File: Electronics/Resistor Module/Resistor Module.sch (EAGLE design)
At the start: 59 parts, among them IC1 74HC595D, IC2 74HC595D, U1 25AA010A

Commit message: Finished layout of resistor module
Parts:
- removed JP5, JP6, JP7, JP8: (no value), Resistor Module Library:M03X24-103240-0-03
- JP1, JP2: value (none) -> M10PASSTHROUGH; device Resistor Module Library:M03X2_535542-3 -> Resistor Module Library:M10PASSTHROUGH
- JP3: device Resistor Module Library:M03X2_535542-3 -> Resistor Module Library:M03X2969973-3
- JP4: device Resistor Module Library:M03X2_535542-3 -> Resistor Module Library:M03X2SMT-M0.1
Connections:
- net N$1 renamed SERIAL_PASS
- removed net N$20 (its old number): IC1A.QG, R19.1
- removed net N$27: IC2A.QE, R25.1
- removed net N$28: IC2A.QF, R26.1
- new net 5V_2: IC2P.VCC, JP2.6
- new net GND_2: IC2P.GND, JP2.5, S10.C-, S11.C-, S12.C-, S13.C-, S7.C-, S8.C-, S9.C-
- new net N$1: IC1A.QH, R26.1
- new net N$13: IC1A.QE, R16.1
- new net N$14: IC1A.QD, R17.1
- new net SERIAL_CLK_2: IC2A.SCK, JP2.9
- new net SERIAL_LATCH_2: IC2A.RCK, JP2.8
- new net SERIAL_MR_L_2: IC2A.SCL, JP2.10
- new net SERIAL_OE_L_2: IC2A.G, JP2.7
- net 5V: now also JP1.6; no longer IC2P.VCC, JP4.1, JP8.5
- net EEPROM_CS_L: now also IC1A.QA; no longer IC2A.QG
- net EEPROM_MISO: now also JP1.4; no longer JP4.4, JP8.4
- net EEPROM_MOSI: now also JP1.2; no longer JP4.2, JP8.6
- net EEPROM_SCK: now also JP1.3; no longer JP4.6, JP8.2
- net GND: now also JP1.5; no longer IC2P.GND, JP4.5, JP8.1, S10.C-, S11.C-, S12.C-, S13.C-, S7.C-, S8.C-, S9.C-
- net N$12: now also IC1A.QF, R15.1; no longer IC1A.QB, R14.1
- net N$16: now also R18.1; no longer R15.1
- net N$17: now also IC1A.QB, R19.1; no longer IC1A.QD, R16.1
- net N$18: now also IC2A.QB, R13.1; no longer IC1A.QE, R17.1
- net N$19: now also IC2A.QC, R25.1; no longer IC1A.QF, R18.1
- net N$2: now also IC1A.QG, R14.1; no longer IC1A.QA, R13.1
- net N$21: now also IC2A.QE, R23.1; no longer IC1A.QH, R20.1
- net N$22: now also IC2A.QF, R22.1; no longer IC2A.QA, R21.1
- net N$23: now also IC2A.QG, R21.1; no longer IC2A.QB, R22.1
- net N$24: now also IC2A.QH, R20.1; no longer IC2A.QC, R23.1
- net RELAY_POST_SHORT: now also S0.C+; no longer S13.C+
- net RELAY_PRE_SHORT: now also S13.C+; no longer S0.C+
- net R_DOWNSTREAM_IN: now also JP3.1, R12.1, R120.1, S12.DC-, S13.DC-; no longer JP3.5, JP3.6, R1.2, S0.DC+, S1.DC+
- net R_DOWNSTREAM_OUT: now also JP4.1, R1.2, S0.DC+, S1.DC+; no longer JP7.1, JP7.2, R12.1, R120.1, S12.DC-, S13.DC-
- net R_UPSTREAM: now also JP3.6, JP4.2; no longer JP3.1, JP3.2, JP7.5, JP7.6
- net SERIAL_CLK: now also JP1.9; no longer IC2A.SCK, JP2.3, JP6.3
- net SERIAL_IN: now also JP3.2; no longer JP2.1
- net SERIAL_LATCH: now also JP1.8; no longer IC2A.RCK, JP2.5, JP6.1
- net SERIAL_MR_L: now also JP1.10; no longer IC2A.SCL, JP2.6, JP6.2
- net SERIAL_OE_L: now also JP1.7; no longer IC2A.G, JP2.4, JP6.4
- net SERIAL_OUT: now also JP4.6; no longer JP6.5
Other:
- note added: "BOTTOM"
- note added: "TOP"
- note removed: "Bottom"
- note removed: "Top"
- moved on the sheet: JP1, JP2, JP3, JP4, R13, R14, R15, R16, R17, R18, R19, R20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

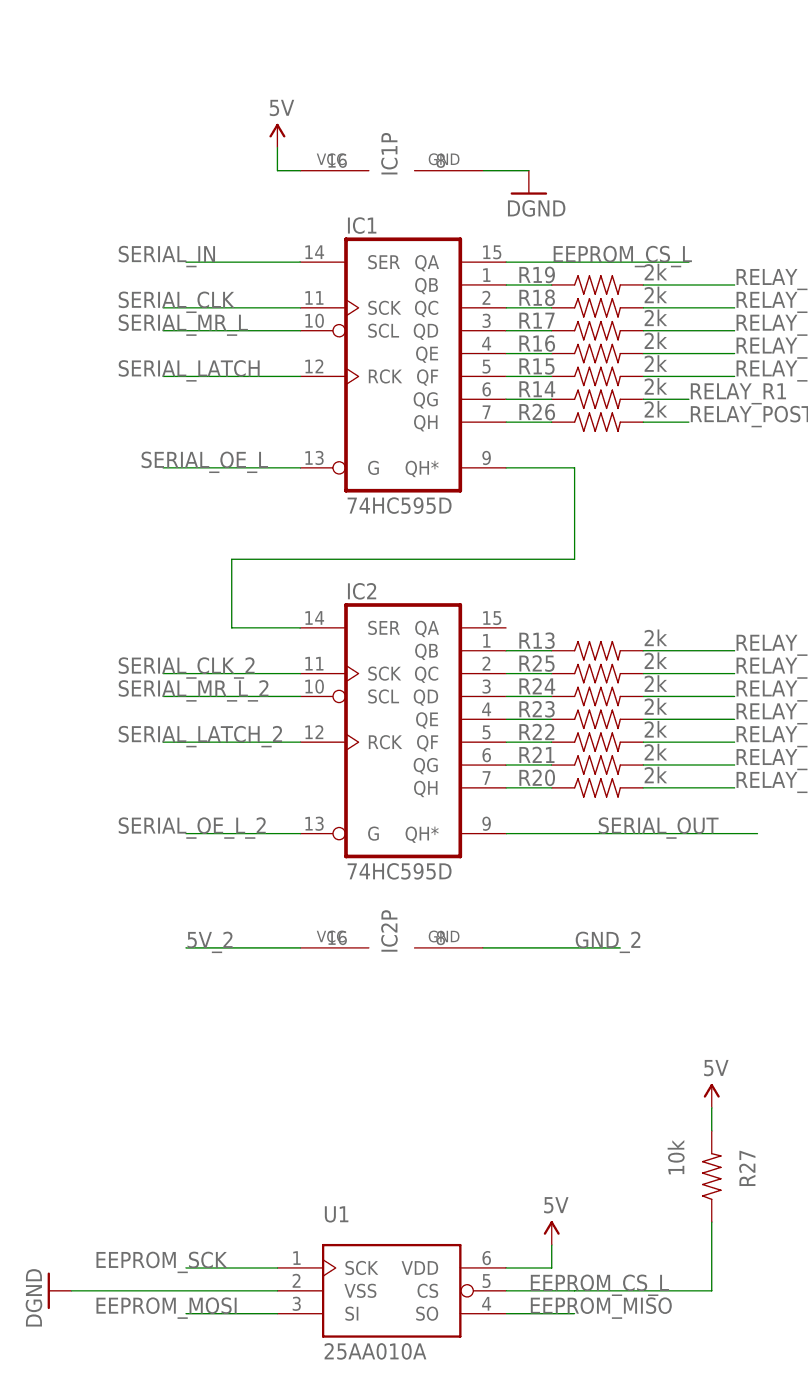
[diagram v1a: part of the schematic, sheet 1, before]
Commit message: Finished layout and updated sketch. Discovered I could fit entire range on a single node if I double back the thing, so gonna do that instead. Who needs modularity when the entire thing fits on one board?
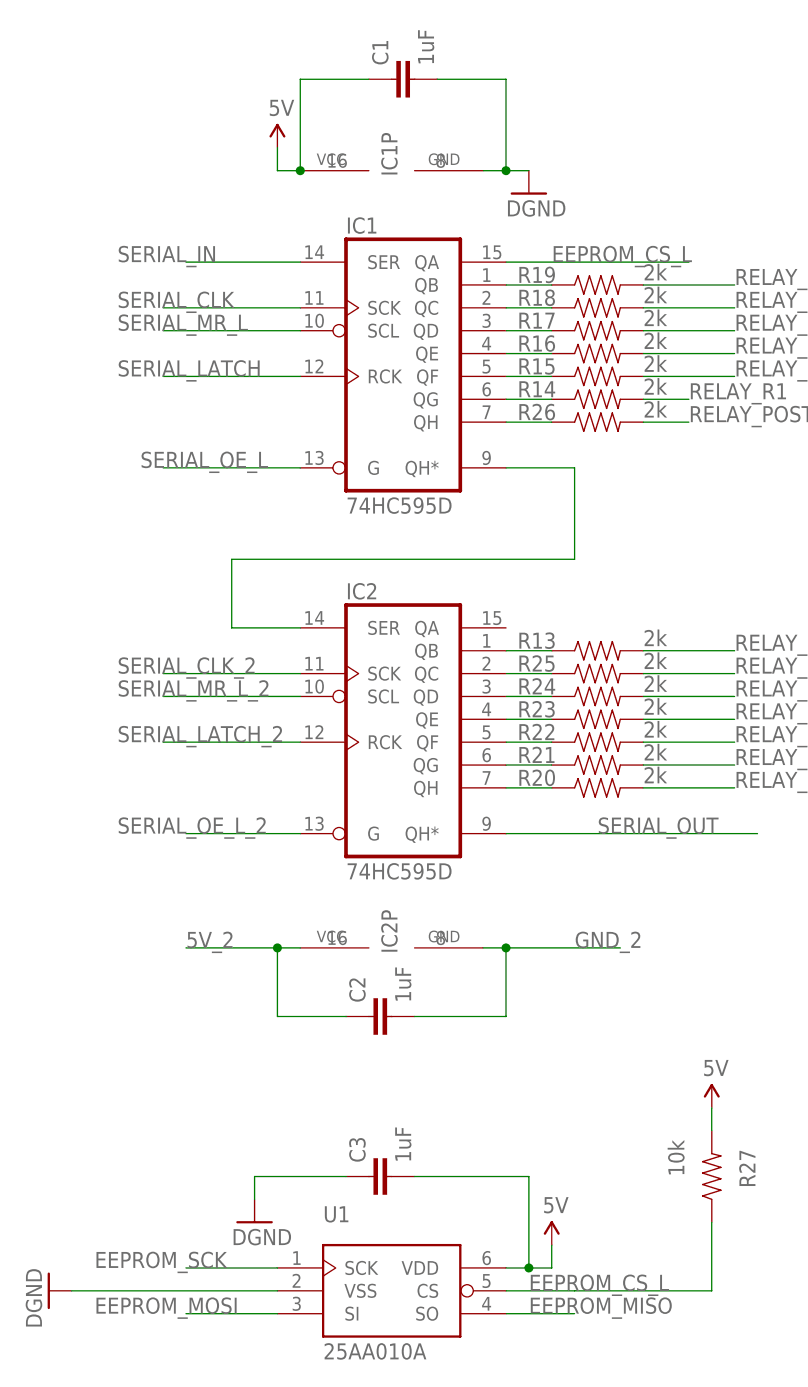
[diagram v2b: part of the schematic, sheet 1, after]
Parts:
- added C1, C2, C3: 1uF, Resistor Module Library:CAP0603-CAP
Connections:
- net 5V: now also C1.1, C3.2
- net 5V_2: now also C2.1
- net GND: now also C1.2, C3.1
- net GND_2: now also C2.2
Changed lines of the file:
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@@
 <part name="SUPPLY6" library="Resistor Module Library" deviceset="5V" device=""/>
 <part name="GND19" library="Resistor Module Library" deviceset="DGND" device=""/>
+<part name="C1" library="Resistor Module Library" deviceset="CAP" device="0603-CAP" value="1uF"/>
+<part name="C2" library="Resistor Module Library" deviceset="CAP" device="0603-CAP" value="1uF"/>
+<part name="C3" library="Resistor Module Library" deviceset="CAP" device="0603-CAP" value="1uF"/>
+<part name="GND2" library="Resistor Module Library" deviceset="DGND" device=""/>
 </parts>
 <sheets>
@@
 </instance>
 <instance part="SUPPLY4" gate="G$1" x="35.56" y="-83.82"/>
+<instance part="C1" gate="G$1" x="2.54" y="30.48" rot="R90"/>
+<instance part="C2" gate="G$1" x="0" y="-73.66" rot="R90"/>
+<instance part="C3" gate="G$1" x="0" y="-91.44" rot="R90"/>
+<instance part="GND2" gate="G$1" x="-15.24" y="-96.52"/>
 </instances>
 <busses>
@@
 <wire x1="-10.16" y1="20.32" x2="-12.7" y2="20.32" width="0.1524" layer="91"/>
 <wire x1="-12.7" y1="20.32" x2="-12.7" y2="22.86" width="0.1524" layer="91"/>
+<pinref part="C1" gate="G$1" pin="1"/>
+<wire x1="-2.54" y1="30.48" x2="-10.16" y2="30.48" width="0.1524" layer="91"/>
+<wire x1="-10.16" y1="30.48" x2="-10.16" y2="20.32" width="0.1524" layer="91"/>
+<junction x="-10.16" y="20.32"/>
 </segment>
 <segment>
 <pinref part="U1" gate="G$1" pin="VDD"/>
-<wire x1="12.7" y1="-101.6" x2="17.78" y2="-101.6" width="0.1524" layer="91"/>
+<wire x1="12.7" y1="-101.6" x2="15.24" y2="-101.6" width="0.1524" layer="91"/>
+<wire x1="15.24" y1="-101.6" x2="17.78" y2="-101.6" width="0.1524" layer="91"/>
 <wire x1="17.78" y1="-101.6" x2="17.78" y2="-99.06" width="0.1524" layer="91"/>
 <pinref part="SUPPLY3" gate="G$1" pin="5V"/>
+<pinref part="C3" gate="G$1" pin="2"/>
+<wire x1="2.54" y1="-91.44" x2="15.24" y2="-91.44" width="0.1524" layer="91"/>
+<wire x1="15.24" y1="-91.44" x2="15.24" y2="-101.6" width="0.1524" layer="91"/>
+<junction x="15.24" y="-101.6"/>
 </segment>
 <segment>
@@
 <pinref part="GND1" gate="G$1" pin="GND"/>
 <pinref part="IC1" gate="P" pin="GND"/>
-<wire x1="15.24" y1="20.32" x2="10.16" y2="20.32" width="0.1524" layer="91"/>
+<wire x1="15.24" y1="20.32" x2="12.7" y2="20.32" width="0.1524" layer="91"/>
+<pinref part="C1" gate="G$1" pin="2"/>
+<wire x1="12.7" y1="20.32" x2="10.16" y2="20.32" width="0.1524" layer="91"/>
+<wire x1="5.08" y1="30.48" x2="12.7" y2="30.48" width="0.1524" layer="91"/>
+<wire x1="12.7" y1="30.48" x2="12.7" y2="20.32" width="0.1524" layer="91"/>
+<junction x="12.7" y="20.32"/>
 </segment>
 <segment>
@@
 <wire x1="-12.7" y1="-104.14" x2="-35.56" y2="-104.14" width="0.1524" layer="91"/>
 <pinref part="GND17" gate="G$1" pin="GND"/>
+</segment>
+<segment>
+<pinref part="C3" gate="G$1" pin="1"/>
+<wire x1="-5.08" y1="-91.44" x2="-15.24" y2="-91.44" width="0.1524" layer="91"/>
+<wire x1="-15.24" y1="-91.44" x2="-15.24" y2="-93.98" width="0.1524" layer="91"/>
+<pinref part="GND2" gate="G$1" pin="GND"/>
 </segment>
 </net>
@@
 <segment>
 <pinref part="IC2" gate="P" pin="VCC"/>
-<wire x1="-10.16" y1="-66.04" x2="-22.86" y2="-66.04" width="0.1524" layer="91"/>
+<wire x1="-10.16" y1="-66.04" x2="-12.7" y2="-66.04" width="0.1524" layer="91"/>
 <label x="-22.86" y="-66.04" size="1.778" layer="95"/>
+<pinref part="C2" gate="G$1" pin="1"/>
+<wire x1="-12.7" y1="-66.04" x2="-22.86" y2="-66.04" width="0.1524" layer="91"/>
+<wire x1="-5.08" y1="-73.66" x2="-12.7" y2="-73.66" width="0.1524" layer="91"/>
+<wire x1="-12.7" y1="-73.66" x2="-12.7" y2="-66.04" width="0.1524" layer="91"/>
+<junction x="-12.7" y="-66.04"/>
 </segment>
 </net>
@@
 <segment>
 <pinref part="IC2" gate="P" pin="GND"/>
-<wire x1="10.16" y1="-66.04" x2="25.4" y2="-66.04" width="0.1524" layer="91"/>
+<wire x1="10.16" y1="-66.04" x2="12.7" y2="-66.04" width="0.1524" layer="91"/>
 <label x="20.32" y="-66.04" size="1.778" layer="95"/>
-</segment>
-</net>
+<pinref part="C2" gate="G$1" pin="2"/>
+<wire x1="12.7" y1="-66.04" x2="25.4" y2="-66.04" width="0.1524" layer="91"/>
+<wire x1="2.54" y1="-73.66" x2="12.7" y2="-73.66" width="0.1524" layer="91"/>
+<wire x1="12.7" y1="-73.66" x2="12.7" y2="-66.04" width="0.1524" layer="91"/>
+<junction x="12.7" y="-66.04"/>
+</segment>
+</net>

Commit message: Reworking resistor module to fit everything on a single module
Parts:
- removed R120: 1k, Resistor Module Library:RESISTOR1206
- removed R80: 100, Resistor Module Library:RESISTOR1206
- removed S0: CPC1002N, Resistor Module Library:CPC1002N
- removed U1: 25AA010A, Resistor Module Library:25AA010A
- added $1_75_$: 25AA010A, Resistor Module Library:25AA010A
- added C4, C5: 1uF, Resistor Module Library:CAP0603-CAP
- added IC3, IC4: 74HC595D, Resistor Module Library:74HC595D
- added R28: 10k, Resistor Module Library:RESISTOR1206
- added R29: 100k, Resistor Module Library:RESISTOR1206
- added R30, R60: 1M, Resistor Module Library:RESISTOR1206
- added R31, R32, R33, R34, R35, R36, R37, R38, R39, R41, R42, R43, R44, R45, R46, R47, R48, R49, R50, R51, R52, R53, R54, R55, R56, R57, R58: 2k, Resistor Module Library:RESISTOR0603-RES
- added R59: 10k, Resistor Module Library:RESISTOR0603-RES
- added R61, R62: 2M, Resistor Module Library:RESISTOR1206
- added R63, R64: 10M, Resistor Module Library:RESISTOR1206
- added S14, S15, S16, S17, S18, S19, S20, S21, S22, S23, S24, S25, S26, S27, S28: CPC1002N, Resistor Module Library:CPC1002N
- JP2: value M10PASSTHROUGH -> (none); device Resistor Module Library:M10PASSTHROUGH -> Resistor Module Library:M03X2969973-3
- JP3: device Resistor Module Library:M03X2969973-3 -> Resistor Module Library:M03X2SMT-M0.1
- JP4: value (none) -> M10PASSTHROUGH; device Resistor Module Library:M03X2SMT-M0.1 -> Resistor Module Library:M10PASSTHROUGH
- R13: value 2k -> 1k; device Resistor Module Library:RESISTOR0603-RES -> Resistor Module Library:RESISTOR1206
- R14, R15: device Resistor Module Library:RESISTOR0603-RES -> Resistor Module Library:RESISTOR1206
- R16, R17: value 2k -> 10k; device Resistor Module Library:RESISTOR0603-RES -> Resistor Module Library:RESISTOR1206
- R18, R19: value 2k -> 20k; device Resistor Module Library:RESISTOR0603-RES -> Resistor Module Library:RESISTOR1206
- R20, R21: value 2k -> 100k; device Resistor Module Library:RESISTOR0603-RES -> Resistor Module Library:RESISTOR1206
- R22, R23: value 2k -> 200k; device Resistor Module Library:RESISTOR0603-RES -> Resistor Module Library:RESISTOR1206
- R24: value 2k -> 1M; device Resistor Module Library:RESISTOR0603-RES -> Resistor Module Library:RESISTOR1206
- R25: value 2k -> 10; device Resistor Module Library:RESISTOR0603-RES -> Resistor Module Library:RESISTOR1206
- R26: value 2k -> 100; device Resistor Module Library:RESISTOR0603-RES -> Resistor Module Library:RESISTOR1206
- R27: value 10k -> 1k; device Resistor Module Library:RESISTOR0603-RES -> Resistor Module Library:RESISTOR1206
- R40: value 10 -> 2k; device Resistor Module Library:RESISTOR1206 -> Resistor Module Library:RESISTOR0603-RES
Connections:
- new net N$26: IC3A.QH, R51.1
- new net N$27: IC3A.QG, R50.1
- new net N$28: IC3A.QF, R49.1
- new net N$29: IC3A.QE, R48.1
- new net N$30: IC3A.QD, R47.1
- new net N$31: IC3A.QC, R46.1
- new net N$32: IC3A.QB, R45.1
- new net N$33: IC4A.QB, R52.1
- new net N$34: IC4A.QC, R53.1
- new net N$35: IC4A.QD, R54.1
- new net N$36: IC4A.QE, R55.1
- new net N$37: IC4A.QF, R56.1
- new net N$38: IC4A.QG, R57.1
- new net N$39: IC4A.QH, R58.1
- new net N$40: R12.1, R13.2, R27.1, S12.DC-, S13.DC+
- new net N$41: R14.1, R15.2, S14.DC-, S15.DC+
- new net N$42: R15.1, R16.2, R28.2, S15.DC-, S16.DC+
- new net N$43: R16.1, R17.2, R28.1, S16.DC-, S17.DC+
- new net N$44: R17.1, R18.2, S17.DC-, S18.DC+
- new net N$45: R18.1, R19.2, S18.DC-, S19.DC+
- new net N$46: R19.1, R20.2, R29.2, S19.DC-, S20.DC+
- new net N$47: R20.1, R21.2, R29.1, S20.DC-, S21.DC+
- new net N$48: R21.1, R22.2, S21.DC-, S22.DC+
- new net N$49: R22.1, R23.2, S22.DC-, S23.DC+
- new net N$50: R23.1, R24.2, R30.2, S23.DC-, S24.DC+
- new net N$51: R13.1, R14.2, S13.DC-, S14.DC+
- new net N$52: R24.1, R30.1, R60.2, S24.DC-, S25.DC+
- new net N$54: R60.1, R61.2, S25.DC-, S26.DC+
- new net N$55: R61.1, R62.2, S26.DC-, S27.DC+
- new net N$56: R62.1, R63.2, R64.2, S27.DC-, S28.DC+
- new net N$57: R63.1, R64.1, S28.DC-
- new net RELAY_R13: S13.C+
- new net RELAY_R14: S14.C+
- new net RELAY_R15: S15.C+
- new net RELAY_R16: S16.C+
- new net RELAY_R17: S17.C+
- new net RELAY_R18: S18.C+
- new net RELAY_R19: S19.C+
- new net RELAY_R20: S20.C+
- new net RELAY_R21: S21.C+
- new net RELAY_R22: S22.C+
- new net RELAY_R23: S23.C+
- new net RELAY_R24: S24.C+
- new net RELAY_R25: S25.C+
- new net RELAY_R26: S26.C+
- new net RELAY_R27: S27.C+
- new net RELAY_R28: S28.C+
- new net R_IN: R1.2, S1.DC+
- new net SERIAL_PASS1: IC2A.QH*, IC3A.SER
- new net SERIAL_PASS2: IC3A.QH*, IC4A.SER
- net 5V: now also $1_75_$.VDD, C3.1, C4.1, C5.2, IC3P.VCC, R59.2; no longer C1.1, C3.2, R27.2, U1.VDD
- net 5V_2: now also C1.1, IC4P.VCC, JP4.6; no longer JP2.6
- net EEPROM_CS_L: now also $1_75_$.CS, IC3A.QA, R59.1; no longer R27.1, U1.CS
- net EEPROM_MISO: now also $1_75_$.SO; no longer U1.SO
- net EEPROM_MOSI: now also $1_75_$.SI; no longer U1.SI
- net EEPROM_SCK: now also $1_75_$.SCK; no longer U1.SCK
- net GND: now also $1_75_$.VSS, C3.2, C4.2, C5.1, IC3P.GND, S10.C-, S11.C-, S12.C-, S13.C-, S14.C-, S15.C-, S16.C-, S17.C-, S18.C-, S19.C-, S20.C-, S21.C-, S22.C-, S23.C-, S24.C-, S25.C-, S26.C-, S27.C-, S28.C-, S7.C-, S8.C-, S9.C-; no longer C1.2, C3.1, S0.C-, U1.VSS
- net GND_2: now also C1.2, IC4P.GND, JP4.5; no longer JP2.5, S10.C-, S11.C-, S12.C-, S13.C-, S7.C-, S8.C-, S9.C-
- net N$1: now also R37.1; no longer R26.1
- net N$12: now also R35.1; no longer R15.1
- net N$13: now also R34.1; no longer R16.1
- net N$14: now also R33.1; no longer R17.1
- net N$15: now also R27.2; no longer R120.2
- net N$16: now also R32.1; no longer R18.1
- net N$17: now also R31.1; no longer R19.1
- net N$18: now also R38.1; no longer R13.1
- net N$19: now also R39.1; no longer R25.1
- net N$2: now also R36.1; no longer R14.1
- net N$20: now also R40.1; no longer R24.1
- net N$21: now also R41.1; no longer R23.1
- net N$22: now also R42.1; no longer R22.1
- net N$23: now also R43.1; no longer R21.1
- net N$24: now also R44.1; no longer R20.1
- net N$4: now also R25.2; no longer R40.2
- net N$5: now also R25.1; no longer R40.1
- net N$8: now also R26.2; no longer R80.2
- net N$9: now also R26.1; no longer R80.1
- net RELAY_POST_SHORT: now also R37.2, R51.2; no longer R26.2, S0.C+
- net RELAY_PRE_SHORT: now also R38.2, R52.2; no longer R13.2, S13.C+
- net RELAY_R1: now also R36.2, R50.2; no longer R14.2
- net RELAY_R10: now also R41.2, R55.2; no longer R23.2
- net RELAY_R11: now also R40.2, R54.2; no longer R24.2
- net RELAY_R12: now also R39.2, R53.2; no longer R25.2
- net RELAY_R2: now also R35.2, R49.2; no longer R15.2
- net RELAY_R3: now also R34.2, R48.2; no longer R16.2
- net RELAY_R4: now also R33.2, R47.2; no longer R17.2
- net RELAY_R5: now also R32.2, R46.2; no longer R18.2
- net RELAY_R6: now also R31.2, R45.2; no longer R19.2
- net RELAY_R7: now also R44.2, R58.2; no longer R20.2
- net RELAY_R8: now also R43.2, R57.2; no longer R21.2
- net RELAY_R9: now also R42.2, R56.2; no longer R22.2
- net R_DOWNSTREAM_IN: now also JP2.1; no longer JP3.1, R12.1, R120.1, S12.DC-, S13.DC-
- net R_DOWNSTREAM_OUT: now also JP3.1; no longer JP4.1, R1.2, S0.DC+, S1.DC+
- net R_UPSTREAM: now also JP2.6, JP3.2; no longer JP3.6, JP4.2, S0.DC-, S13.DC+
- net SERIAL_CLK: now also IC3A.SCK
- net SERIAL_CLK_2: now also IC4A.SCK, JP4.9; no longer JP2.9
- net SERIAL_IN: now also JP2.2; no longer JP3.2
- net SERIAL_LATCH: now also IC3A.RCK
- net SERIAL_LATCH_2: now also IC4A.RCK, JP4.8; no longer JP2.8
- net SERIAL_MR_L: now also IC3A.SCL
- net SERIAL_MR_L_2: now also IC4A.SCL, JP4.10; no longer JP2.10
- net SERIAL_OE_L: now also IC3A.G
- net SERIAL_OE_L_2: now also IC4A.G, JP4.7; no longer JP2.7
- net SERIAL_OUT: now also JP3.6; no longer IC2A.QH*, JP4.6
